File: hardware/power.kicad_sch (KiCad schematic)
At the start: 9 parts, among them U201 SPX3819M5-L-3-3

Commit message: WIP pcb layout
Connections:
- net BP: now reaches C204.1, U201.4 (BP)
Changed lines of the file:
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@@
+		)
+	)
+	(label "BP"
+		(at 116.84 48.26 0)
+		(fields_autoplaced yes)
+		(effects
+			(font
+				(size 1.27 1.27)
+			)
+			(justify left bottom)
 		)
 	)

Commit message: Finished the pcb layout
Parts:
- D201: MPN C72043 -> C12624
- U201: Rotation Offset (none) -> 90
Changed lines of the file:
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@@
 			)
 		)
-		(property "MPN" "C72043"
+		(property "MPN" "C12624"
 			(at 143.51 52.07 0)
 			(effects
@@
 			(at 107.95 48.26 0)
 			(effects
+				(font
+					(size 1.27 1.27)
+				)
+				(hide yes)
+			)
+		)
+		(property "Rotation Offset" "90"
+			(at 107.95 48.26 0)
+			(effects

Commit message: release: v0.1
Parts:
- D201: footprint LED_SMD:LED_0603_1608Metric -> LED_SMD:LED_0805_2012Metric; MPN C12624 -> C2297
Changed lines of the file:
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@@
 	(title_block
 		(title "Radiator Booster")
-		(date "2024-11-17")
+		(date "2025-01-19")
 		(rev "0.1")
 		(company "LP")
@@
 			)
 		)
-		(property "Footprint" "LED_SMD:LED_0603_1608Metric"
+		(property "Footprint" "LED_SMD:LED_0805_2012Metric"
 			(at 143.51 52.07 0)
 			(effects
@@
 			)
 		)
-		(property "MPN" "C12624"
+		(property "MPN" "C2297"
 			(at 143.51 52.07 0)
 			(effects

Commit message: Started work on rev 0.2
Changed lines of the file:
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@@
 (kicad_sch
-	(version 20231120)
+	(version 20250114)
 	(generator "eeschema")
-	(generator_version "8.0")
+	(generator_version "9.0")
 	(paper "A4")
 	(title_block
 		(title "Radiator Booster")
-		(date "2025-01-19")
-		(rev "0.1")
+		(date "2025-03-08")
+		(rev "0.2")
 		(company "LP")
 	)
+	(text "Input Filter"
+		(exclude_from_sim no)
+		(at 22.86 31.75 0)
+		(effects
+			(font
+				(size 2.54 2.54)
+			)
+			(justify left bottom)
+		)
+	)
+	(text "* Vin(MAX)=5V\n* Iout(MAX)=500mA"
+		(exclude_from_sim no)
+		(at 80.01 35.814 0)
+		(effects
+			(font
+				(size 1.27 1.27)
+			)
+			(justify left bottom)
+		)
+	)
+	(text "VBUS power comes from USB Type C Connector\n"
+		(exclude_from_sim no)
+		(at 22.86 77.47 0)
+		(effects
+			(font
+				(size 1.27 1.27)
+			)
+			(justify left bottom)
+		)
+	)
+	(text "L(ESR)=0.15R\nI(DC)=500mA (esp) + Nx150mA per PWM Fan"
+		(exclude_from_sim no)
+		(at 23.114 36.576 0)
+		(effects
+			(font
+				(size 1.27 1.27)
+			)
+			(justify left bottom)
+		)
+	)
+	(text "3.3V Supply (LDO)\n"
+		(exclude_from_sim no)
+		(at 80.01 32.004 0)
+		(effects
+			(font
+				(size 2.54 2.54)
+			)
+			(justify left bottom)
+		)
+	)
+	(text "VBUS power comes from USB Type C Connector\n"
+		(exclude_from_sim no)
+		(at 77.47 77.47 0)
+		(effects
+			(font
+				(size 1.27 1.27)
+			)
+			(justify left bottom)
+		)
+	)
 	(junction
 		(at 82.55 45.72)
@@
 			(width 0)
 			(type default)
-		)
-	)
-	(text "Input Filter"
-		(exclude_from_sim no)
-		(at 22.86 31.75 0)
-		(effects
-			(font
-				(size 2.54 2.54)
-			)
-			(justify left bottom)
-		)
-	)
-	(text "* Vin(MAX)=5V\n* Iout(MAX)=500mA"
-		(exclude_from_sim no)
-		(at 80.01 35.814 0)
-		(effects
-			(font
-				(size 1.27 1.27)
-			)
-			(justify left bottom)
-		)
-	)
-	(text "VBUS power comes from USB Type C Connector\n"
-		(exclude_from_sim no)
-		(at 22.86 77.47 0)
-		(effects
-			(font
-				(size 1.27 1.27)
-			)
-			(justify left bottom)
-		)
-	)
-	(text "L(ESR)=0.15R\nI(DC)=500mA (esp) + Nx150mA per PWM Fan"
-		(exclude_from_sim no)
-		(at 23.114 36.576 0)
-		(effects
-			(font
-				(size 1.27 1.27)
-			)
-			(justify left bottom)
-		)
-	)
-	(text "3.3V Supply (LDO)\n"
-		(exclude_from_sim no)
-		(at 80.01 32.004 0)
-		(effects
-			(font
-				(size 2.54 2.54)
-			)
-			(justify left bottom)
-		)
-	)
-	(text "VBUS power comes from USB Type C Connector\n"
-		(exclude_from_sim no)
-		(at 77.47 77.47 0)
-		(effects
-			(font
-				(size 1.27 1.27)
-			)
-			(justify left bottom)
 		)
 	)
 	(label "BP"
 		(at 116.84 48.26 0)
-		(fields_autoplaced yes)
-		(effects
-			(font
+		(effects
+			(font

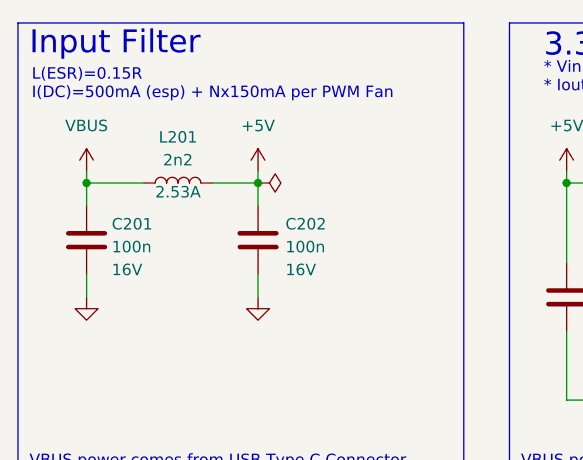
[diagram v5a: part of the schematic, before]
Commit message: Updated matching network. Changed inductor for all filter for bom sonsolidation after matching network changes
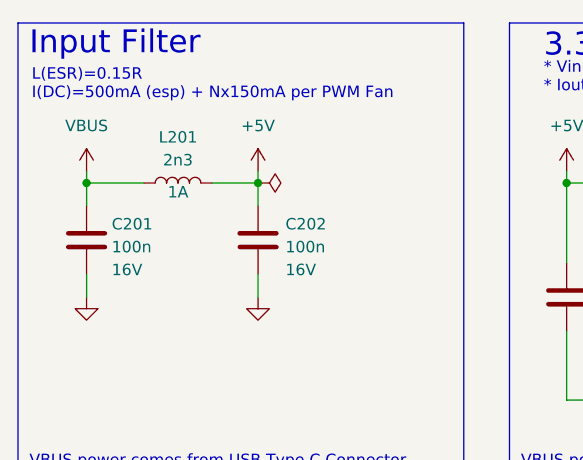
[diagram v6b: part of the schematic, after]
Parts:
- L201: value 2n2 -> 2n3; MPN C412264 -> C412340; Rating 2.53A -> 1A
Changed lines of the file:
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@@
 			)
 		)
-		(property "Value" "2n2"
+		(property "Value" "2n3"
 			(at 39.37 43.18 90)
 			(effects
@@
 			)
 		)
-		(property "Rating" "2.53A"
+		(property "Rating" "1A"
 			(at 39.37 46.736 90)
 			(effects
@@
 			)
 		)
-		(property "MPN" "C412264"
+		(property "MPN" "C412340"
 			(at 39.37 45.72 0)
 			(effects
